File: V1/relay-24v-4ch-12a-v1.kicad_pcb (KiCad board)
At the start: 2 copper layers, 53 x 67.8 mm, 22 parts, among them J1 DG141V-2.54-6P, J2 DB142V-5.08-8P, K1 G5PZ-1A, K2 G5PZ-1A, K3 G5PZ-1A, K4 G5PZ-1A

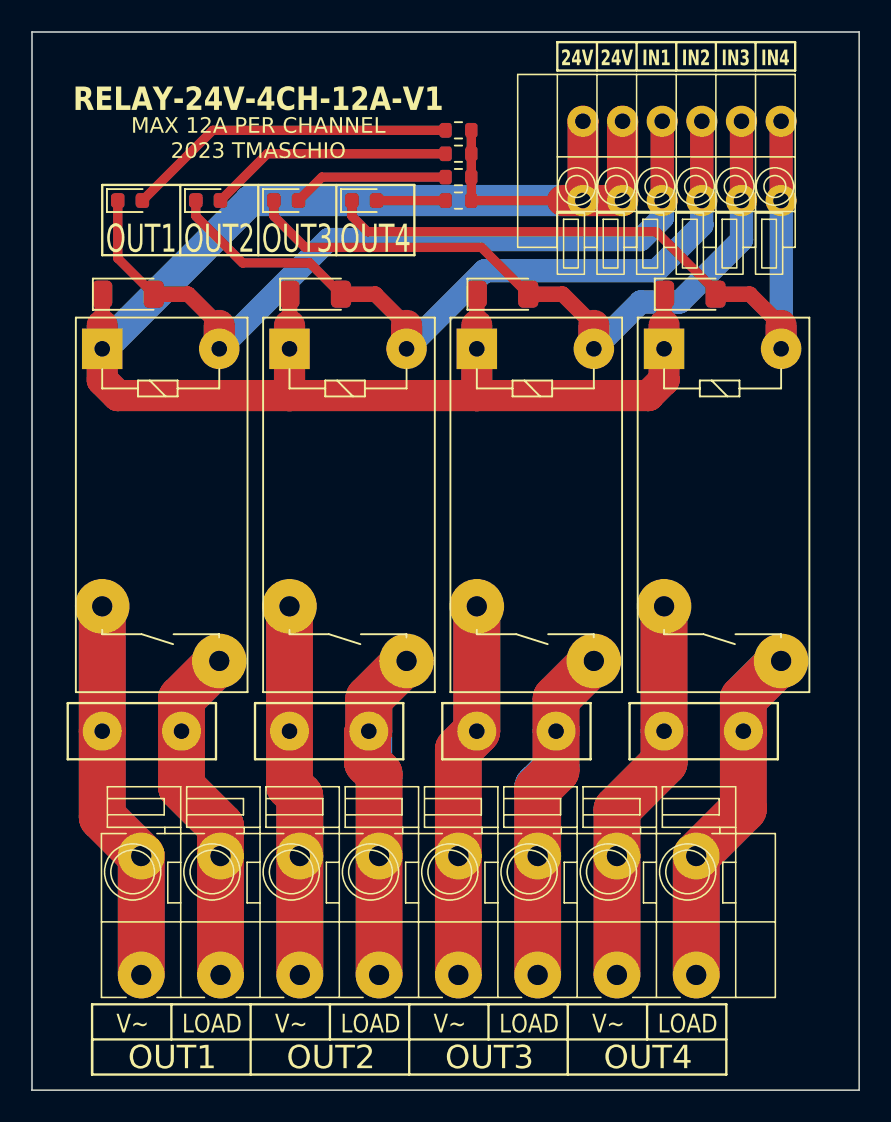
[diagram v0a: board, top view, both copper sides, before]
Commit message: Updated connectors
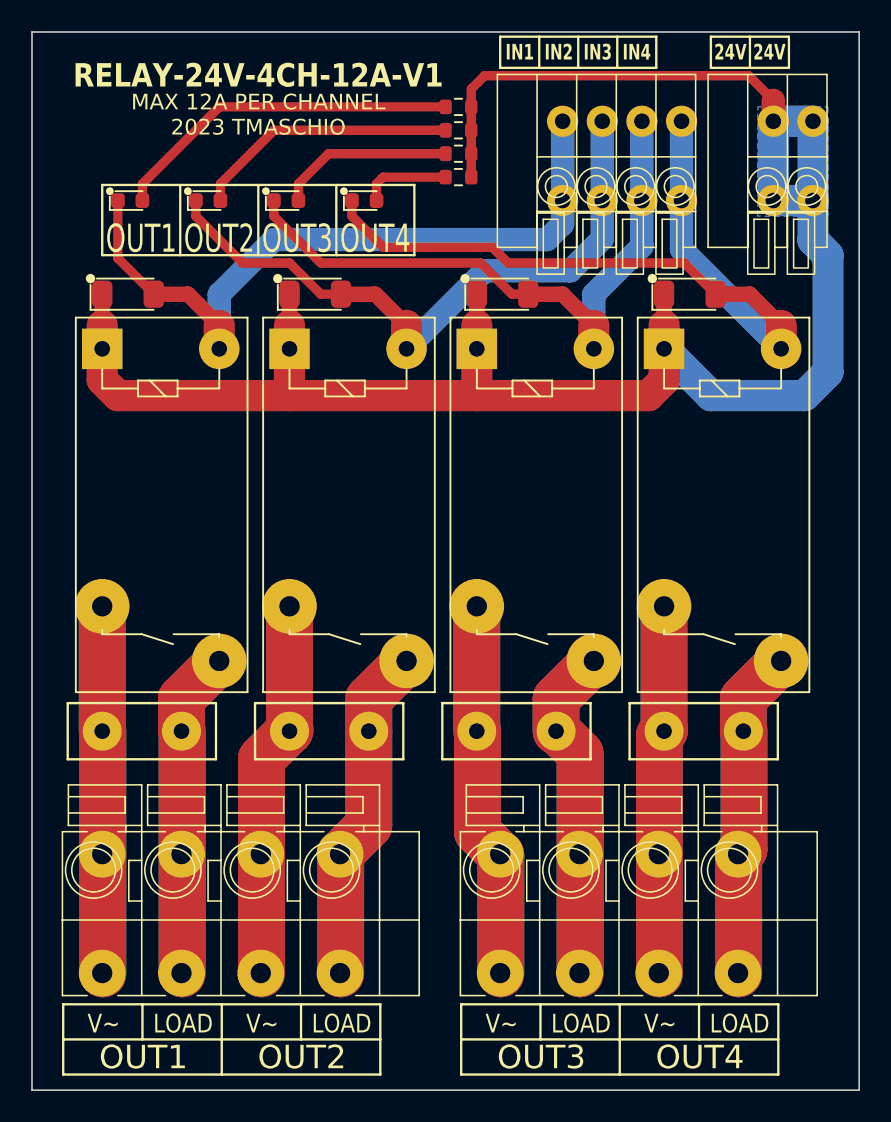
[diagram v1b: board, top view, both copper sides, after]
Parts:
- added J3: DB142V-5.08-4P, Tales:TerminalBlock_Dibo_DB142V-5.08-4P_1x04_P5.08mm_Vertical, F.Cu at (129.5, 122.5)
- added J4: DB142V-5.08-4P, Tales:TerminalBlock_Dibo_DB142V-5.08-4P_1x04_P5.08mm_Vertical, F.Cu at (155.0, 122.5)
- J1: value DG141V-2.54-6P -> DB141V-2.54-2P; footprint Tales:TerminalBlock_Dibo_DB141V-2.54-6P_1x06_P2.54mm_Vertical -> Tales:TerminalBlock_Dibo_DB141V-2.54-2P_1x02_P2.54mm_Vertical
- J2: value DB142V-5.08-8P -> DB141V-2.54-4P; footprint Tales:TerminalBlock_Dibo_DB142V-5.08-8P_1x08_P5.08mm_Vertical -> Tales:TerminalBlock_Dibo_DB141V-2.54-4P_1x04_P2.54mm_Vertical
- R1, R2, R3, R4: value 5k6/100mW -> 6k8/100mW
- moved J2 64.7 mm to (166.6, 67.9), turned to 180 degrees
- moved J1 2.04 mm to (175.0, 67.9)
- moved R1 1.50 mm to (152.3, 67.0)
- moved R2 1.50 mm to (152.3, 68.5)
- moved R3 1.50 mm to (152.3, 70.0)
- moved R4 1.50 mm to (152.3, 71.5)
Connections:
- J1 pad 1: Net-(D7-K) -> +24V
- J1 pad 2: Net-(D5-K) -> +24V
- J2 pad 1: Net-(J2-Pin_1) -> Net-(D7-K)
- J2 pad 2: Net-(J2-Pin_2) -> Net-(D5-K)
- J2 pad 3: Net-(J2-Pin_3) -> Net-(D3-K)
- J2 pad 4: Net-(J2-Pin_4) -> Net-(D1-K)
- K1 pad 2: Net-(J2-Pin_1) -> Net-(J3-Pin_1)
- K1 pad 3: Net-(J2-Pin_2) -> Net-(J3-Pin_2)
- K2 pad 2: Net-(J2-Pin_3) -> Net-(J3-Pin_3)
- K2 pad 3: Net-(J2-Pin_4) -> Net-(J3-Pin_4)
- K3 pad 2: Net-(J2-Pin_5) -> Net-(J4-Pin_1)
- K3 pad 3: Net-(J2-Pin_6) -> Net-(J4-Pin_2)
- K4 pad 2: Net-(J2-Pin_7) -> Net-(J4-Pin_3)
- K4 pad 3: Net-(J2-Pin_8) -> Net-(J4-Pin_4)
- RV1 pad 1: Net-(J2-Pin_1) -> Net-(J3-Pin_1)
- RV1 pad 2: Net-(J2-Pin_2) -> Net-(J3-Pin_2)
- RV2 pad 1: Net-(J2-Pin_3) -> Net-(J3-Pin_3)
- RV2 pad 2: Net-(J2-Pin_4) -> Net-(J3-Pin_4)
- RV3 pad 1: Net-(J2-Pin_5) -> Net-(J4-Pin_1)
- RV3 pad 2: Net-(J2-Pin_6) -> Net-(J4-Pin_2)
- RV4 pad 1: Net-(J2-Pin_7) -> Net-(J4-Pin_3)
- RV4 pad 2: Net-(J2-Pin_8) -> Net-(J4-Pin_4)
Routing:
- net Net-(J2-Pin_7): track 49.7 -> 0.00 mm
- net Net-(J2-Pin_1): track 49.3 -> 0.00 mm
- net Net-(J3-Pin_3): track 0.00 -> 48.8 mm
- net Net-(J4-Pin_1): track 0.00 -> 48.5 mm
- net Net-(J2-Pin_5): track 48.2 -> 0.00 mm
- net Net-(J2-Pin_3): track 47.8 -> 0.00 mm
- net Net-(J4-Pin_3): track 0.00 -> 47.5 mm
- net Net-(J3-Pin_1): track 0.00 -> 47.2 mm
- net Net-(J2-Pin_8): track 44.7 -> 0.00 mm
- net Net-(J2-Pin_2): track 44.3 -> 0.00 mm
- net Net-(J3-Pin_4): track 0.00 -> 43.5 mm
- net Net-(J4-Pin_2): track 0.00 -> 43.5 mm
- net Net-(J2-Pin_6): track 43.2 -> 0.00 mm
- net Net-(J2-Pin_4): track 42.9 -> 0.00 mm
- net Net-(J4-Pin_4): track 0.00 -> 42.5 mm
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- added copper zone on B.Cu, net +24V

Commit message: Revision before manufacturing
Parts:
- D1, D3, D5, D7: value GREEN -> WHITE
- R1, R2, R3, R4: value 6k8/100mW -> 10k/100mW
- moved K1 10.7 mm to (133.2, 92.5)
- moved K2 10.7 mm to (145.2, 92.5)
- moved K3 10.7 mm to (157.2, 92.5)
- moved K4 10.7 mm to (169.2, 92.5)
- moved J3 8.61 mm to (137.2, 118.8)
- moved J4 8.61 mm to (162.8, 118.8)
- moved J2 4.65 mm to (162.8, 70.5)
- moved J1 2.88 mm to (173.8, 70.5)
- moved RV1 2.75 mm to (132.2, 107.0)
- moved RV2 2.75 mm to (144.2, 107.0)
- moved RV3 2.75 mm to (156.2, 107.0)
- moved RV4 2.75 mm to (168.2, 107.0)
- moved D2 0.15 mm to (131.0, 79.0)
- moved D4 0.15 mm to (143.0, 79.0)
- moved D6 0.15 mm to (155.0, 79.0)
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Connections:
- net Net-(D1-A) renamed /LED1
- net Net-(D1-K) renamed /IN1
- net Net-(D3-A) renamed /LED2
- net Net-(D3-K) renamed /IN2
- net Net-(D5-A) renamed /LED3
- net Net-(D5-K) renamed /IN3
- net Net-(D7-A) renamed /LED4
- net Net-(D7-K) renamed /IN4
- net Net-(J3-Pin_1) renamed /OUT1PW
- net Net-(J3-Pin_2) renamed /OUT1LD
- net Net-(J3-Pin_3) renamed /OUT2PW
- net Net-(J3-Pin_4) renamed /OUT2LD
- net Net-(J4-Pin_1) renamed /OUT3PW
- net Net-(J4-Pin_2) renamed /OUT3LD
- net Net-(J4-Pin_3) renamed /OUT4PW
- net Net-(J4-Pin_4) renamed /OUT4LD
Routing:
- net +24V: track 127.2 -> 115.2 mm
- net /IN2: track 41.9 -> 43.7 mm
- net /IN1: track 47.4 -> 46.8 mm
- net /LED3: track 11.3 -> 10.7 mm
- net /LED4: track 5.68 -> 5.08 mm
- net /LED2: track 16.9 -> 16.3 mm
- net /LED1: track 22.5 -> 21.9 mm
- added copper zone on F.Cu, net +24V
- removed copper zone on B.Cu, net +24V
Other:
- rule pad_to_mask_clearance: 0 -> 0.1

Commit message: Review before fabrication
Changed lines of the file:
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@@
 			(unlocked yes)
 			(layer "F.SilkS")
-			(hide yes)
 			(effects
 				(font
@@
 			)
 		)
-		(property "JLCPCB BOM" "0"
+		(property "JLCPCB BOM" "1"
 			(at 83 248 0)
 			(layer "F.Fab")
@@
 			)
 		)
-		(property "Mfr PN" "G5PZ-1A"
+		(property "Mfr PN" "G5PZ-1A-E DC24V"
 			(at 83 248 0)
 			(layer "F.Fab")
@@
 			)
 		)
-		(property "Vendor" "Mouser"
+		(property "Vendor" "JLCPCB"
 			(at 83 248 0)
 			(layer "F.Fab")
@@
 			)
 		)
-		(property "Vendor PN" "653-G5PZ-1ADC24"
+		(property "Vendor PN" "C6719448"
 			(at 83 248 0)
 			(layer "F.Fab")
@@
 			)
 		)
+		(property "LCSC Part #" "C6719448"
+			(at 0 0 270)
+			(unlocked yes)
+			(layer "F.Fab")
+			(hide yes)
+			(effects
+				(font
+					(size 1 1)
+					(thickness 0.15)
+				)
+			)
+		)
 		(property ki_fp_filters "Relay*SPST*Omron*G5PZ*")
 		(sheetname "/")
@@
 			(at 6 -1.25 0)
 			(layer "F.SilkS")
-			(hide yes)
 			(effects
 				(font
@@
 			)
 		)
+		(property "LCSC Part #" "C2898744"
+			(at 0 0 180)
+			(unlocked yes)
+			(layer "F.Fab")
+			(hide yes)
+			(effects
+				(font
+					(size 1 1)
+					(thickness 0.15)
+				)
+			)
+		)
+		(property "Mfr" "DORABO"
+			(at 0 0 180)
+			(unlocked yes)
+			(layer "F.Fab")
+			(hide yes)
+			(effects
+				(font
+					(size 1 1)
+					(thickness 0.15)
+				)
+			)
+		)
+		(property "Mfr PN" "DB141V-2.54-2P-GN"
+			(at 0 0 180)
+			(unlocked yes)
+			(layer "F.Fab")
+			(hide yes)
+			(effects
+				(font
+					(size 1 1)
+					(thickness 0.15)
+				)
+			)
+		)
+		(property "Vendor PN" "C2898744"
+			(at 0 0 180)
+			(unlocked yes)
+			(layer "F.Fab")
+			(hide yes)
+			(effects
+				(font
+					(size 1 1)
+					(thickness 0.15)
+				)
+			)
+		)
 		(property ki_fp_filters "Connector*:*_1x??_*")
 		(sheetname "/")
@@
 			)
 		)
-		(property "JLCPCB BOM" "0"
+		(property "JLCPCB BOM" "1"
 			(at 71 236 0)
 			(layer "F.Fab")
@@
 			)
 		)
-		(property "Mfr PN" "G5PZ-1A"
+		(property "Mfr PN" "G5PZ-1A-E DC24V"
 			(at 71 236 0)
 			(layer "F.Fab")
@@
 			)
 		)
-		(property "Vendor" "Mouser"
+		(property "Vendor" "JLCPCB"
 			(at 71 236 0)
 			(layer "F.Fab")
@@
 			)
 		)
-		(property "Vendor PN" "653-G5PZ-1ADC24"
+		(property "Vendor PN" "C6719448"
 			(at 71 236 0)
 			(layer "F.Fab")
@@
 			)
 		)
+		(property "LCSC Part #" "C6719448"
+			(at 0 0 270)
+			(unlocked yes)
+			(layer "F.Fab")
+			(hide yes)
+			(effects
+				(font
+					(size 1 1)
+					(thickness 0.15)
+				)
+			)
+		)
 		(property ki_fp_filters "Relay*SPST*Omron*G5PZ*")
 		(sheetname "/")
@@
 			(at 6 -1.25 0)
 			(layer "F.SilkS")
-			(hide yes)
 			(effects
 				(font
@@
 			(at 6 -1.25 0)
 			(layer "F.SilkS")
-			(hide yes)
 			(effects
 				(font
@@
 			(unlocked yes)
 			(layer "F.SilkS")
-			(hide yes)
 			(effects
 				(font
@@
 			)
 		)
+		(property "LCSC Part #" "C2898746"
+			(at 0 0 180)
+			(unlocked yes)
+			(layer "F.Fab")
+			(hide yes)
+			(effects
+				(font
+					(size 1 1)
+					(thickness 0.15)
+				)
+			)
+		)
+		(property "Mfr" "DORABO"
+			(at 0 0 180)
+			(unlocked yes)
+			(layer "F.Fab")
+			(hide yes)
+			(effects
+				(font
+					(size 1 1)
+					(thickness 0.15)
+				)
+			)
+		)
+		(property "Mfr PN" "DB141V-2.54-4P-GN"
+			(at 0 0 180)
+			(unlocked yes)
+			(layer "F.Fab")
+			(hide yes)
+			(effects
+				(font
+					(size 1 1)
+					(thickness 0.15)
+				)
+			)
+		)
+		(property "Vendor PN" "C2898746"
+			(at 0 0 180)
+			(unlocked yes)
+			(layer "F.Fab")
+			(hide yes)
+			(effects
+				(font
+					(size 1 1)
+					(thickness 0.15)
+				)
+			)
+		)
 		(property ki_fp_filters "Connector*:*_1x??_*")
 		(sheetname "/")
@@
 			)
 		)
-		(property "JLCPCB BOM" "0"
+		(property "JLCPCB BOM" "1"
 			(at 59 224 0)
 			(layer "F.Fab")
@@
 			)
 		)
-		(property "Mfr PN" "G5PZ-1A"
+		(property "Mfr PN" "G5PZ-1A-E DC24V"
 			(at 59 224 0)
 			(layer "F.Fab")
@@
 			)
 		)
-		(property "Vendor" "Mouser"
+		(property "Vendor" "JLCPCB"
 			(at 59 224 0)
 			(layer "F.Fab")
@@
 			)
 		)
-		(property "Vendor PN" "653-G5PZ-1ADC24"
+		(property "Vendor PN" "C6719448"
 			(at 59 224 0)
 			(layer "F.Fab")
@@
 			)
 		)
+		(property "LCSC Part #" "C6719448"
+			(at 0 0 270)
+			(unlocked yes)
+			(layer "F.Fab")
+			(hide yes)
+			(effects
+				(font
+					(size 1 1)
+					(thickness 0.15)
+				)
+			)
+		)
 		(property ki_fp_filters "Relay*SPST*Omron*G5PZ*")
 		(sheetname "/")
@@
 			)
 		)
-		(property "JLCPCB BOM" "0"
+		(property "JLCPCB BOM" "1"
 			(at 47 212 0)
 			(layer "F.Fab")
@@
 			)
 		)
-		(property "Mfr PN" "G5PZ-1A"
+		(property "Mfr PN" "G5PZ-1A-E DC24V"
 			(at 47 212 0)
 			(layer "F.Fab")
@@
 			)
 		)
-		(property "Vendor" "Mouser"
+		(property "Vendor" "JLCPCB"
 			(at 47 212 0)
 			(layer "F.Fab")
@@
 			)
 		)
-		(property "Vendor PN" "653-G5PZ-1ADC24"
+		(property "Vendor PN" "C6719448"
 			(at 47 212 0)
 			(layer "F.Fab")
@@
 			)
 		)
+		(property "LCSC Part #" "C6719448"
+			(at 0 0 270)
+			(unlocked yes)
+			(layer "F.Fab")
+			(hide yes)
+			(effects
+				(font
+					(size 1 1)
+					(thickness 0.15)
+				)
+			)
+		)
 		(property ki_fp_filters "Relay*SPST*Omron*G5PZ*")
 		(sheetname "/")
@@
 			(at 6 -1.25 0)
 			(layer "F.SilkS")
-			(hide yes)
 			(effects
 				(font
@@
 		(effects
 			(font
-				(size 1.5 1.5)
+				(size 1.4 1.3)
 				(thickness 0.2)
 			)
@@
 		(effects
 			(font
-				(size 1.5 1.5)
+				(size 1.4 1.3)
 				(thickness 0.2)
 			)
@@
 		(effects
 			(font
-				(size 1.5 1.5)
+				(size 1.4 1.3)
 				(thickness 0.2)
 			)
@@
 		(effects
 			(font
-				(size 1.5 1.5)
+				(size 1.4 1.3)
 				(thickness 0.2)
 			)

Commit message: Revising before manufacturing.
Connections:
- net /OUT1PW renamed /OUT1LN
- net /OUT2PW renamed /OUT2LN
- net /OUT3PW renamed /OUT3LN
- net /OUT4PW renamed /OUT4LN
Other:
- board text added: "LINE"
- board text removed: "V~"
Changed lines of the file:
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@@
 	(net 8 "/LED4")
 	(net 9 "/IN4")
-	(net 10 "/OUT1PW")
+	(net 10 "/OUT2LN")
 	(net 11 "/OUT2LD")
 	(net 12 "/OUT1LD")
-	(net 13 "/OUT2PW")
+	(net 13 "/OUT1LN")
 	(net 14 "/OUT3LD")
-	(net 15 "/OUT3PW")
+	(net 15 "/OUT3LN")
 	(net 16 "/OUT4LD")
-	(net 17 "/OUT4PW")
+	(net 17 "/OUT4LN")
 	(footprint "Tales:TerminalBlock_Dibo_DB142V-5.08-4P_1x04_P5.08mm_Vertical"
 		(layer "F.Cu")
@@
 			(layers "*.Cu" "*.Mask")
 			(remove_unused_layers no)
-			(net 15 "/OUT3PW")
+			(net 15 "/OUT3LN")
 			(pinfunction "Pin_1")
 			(pintype "passive")
@@
 			(layers "*.Cu" "*.Mask")
 			(remove_unused_layers no)
-			(net 15 "/OUT3PW")
+			(net 15 "/OUT3LN")
 			(pinfunction "Pin_1")
 			(pintype "passive")
@@
 			(layers "*.Cu" "*.Mask")
 			(remove_unused_layers no)
-			(net 17 "/OUT4PW")
+			(net 17 "/OUT4LN")
 			(pinfunction "Pin_3")
 			(pintype "passive")
@@
 			(layers "*.Cu" "*.Mask")
 			(remove_unused_layers no)
-			(net 17 "/OUT4PW")
+			(net 17 "/OUT4LN")
 			(pinfunction "Pin_3")
 			(pintype "passive")
@@
 			(layers "*.Cu" "*.Mask")
 			(remove_unused_layers no)
-			(net 17 "/OUT4PW")
+			(net 17 "/OUT4LN")
 			(pintype "passive")
 		)
@@
 			(layers "*.Cu" "*.Mask")
 			(remove_unused_layers no)
-			(net 10 "/OUT1PW")
+			(net 13 "/OUT1LN")
 			(pintype "passive")
 		)
@@
 			(layers "*.Cu" "*.Mask")
 			(remove_unused_layers no)
-			(net 15 "/OUT3PW")
+			(net 15 "/OUT3LN")
 			(pintype "passive")
 		)
@@
 			(layers "*.Cu" "*.Mask")
 			(remove_unused_layers no)
-			(net 17 "/OUT4PW")
+			(net 17 "/OUT4LN")
 			(pintype "passive")
 		)
@@
 			(layers "*.Cu" "*.Mask")
 			(remove_unused_layers no)
-			(net 13 "/OUT2PW")
+			(net 10 "/OUT2LN")
 			(pintype "passive")
 		)
@@
 			(layers "*.Cu" "*.Mask")
 			(remove_unused_layers no)
-			(net 10 "/OUT1PW")
+			(net 13 "/OUT1LN")
 			(pinfunction "Pin_1")
 			(pintype "passive")
@@
 			(layers "*.Cu" "*.Mask")
 			(remove_unused_layers no)
-			(net 10 "/OUT1PW")
+			(net 13 "/OUT1LN")
 			(pinfunction "Pin_1")
 			(pintype "passive")
@@
 			(layers "*.Cu" "*.Mask")
 			(remove_unused_layers no)
-			(net 13 "/OUT2PW")
+			(net 10 "/OUT2LN")
 			(pinfunction "Pin_3")
 			(pintype "passive")
@@
 			(layers "*.Cu" "*.Mask")
 			(remove_unused_layers no)
-			(net 13 "/OUT2PW")
+			(net 10 "/OUT2LN")
 			(pinfunction "Pin_3")
 			(pintype "passive")
@@
 			(layers "*.Cu" "*.Mask")
 			(remove_unused_layers no)
-			(net 13 "/OUT2PW")
+			(net 10 "/OUT2LN")
 			(pintype "passive")
 		)
@@
 			(layers "*.Cu" "*.Mask")
 			(remove_unused_layers no)
-			(net 10 "/OUT1PW")
+			(net 13 "/OUT1LN")
 			(pintype "passive")
 		)
@@
 			(layers "*.Cu" "*.Mask")
 			(remove_unused_layers no)
-			(net 15 "/OUT3PW")
+			(net 15 "/OUT3LN")
 			(pintype "passive")
 		)
@@
 		)
 	)
-	(gr_text "V~"
+	(gr_text "LINE"
 		(at 155.1 125.75 0)
 		(layer "F.SilkS")
@@
 		)
 	)
-	(gr_text "V~"
+	(gr_text "LINE"
 		(at 129.6 125.75 0)
 		(layer "F.SilkS")
@@
 		)
 	)
-	(gr_text "V~"
+	(gr_text "LINE"
 		(at 165.26 125.75 0)
 		(layer "F.SilkS")
@@
 		)
 	)
-	(gr_text "V~"
+	(gr_text "LINE"
 		(at 139.76 125.75 0)
 		(layer "F.SilkS")
@@
 	)
 	(segment
-		(start 129.63 114.94)
-		(end 129.63 107.08)
+		(start 139.79 122.56)
+		(end 139.79 114.94)
 		(width 3)
 		(layer "F.Cu")
@@
 	)
 	(segment
-		(start 129.71 107)
-		(end 129.71 99.21)
+		(start 139.79 114.94)
+		(end 139.79 108.92)
 		(width 3)
 		(layer "F.Cu")
@@
 	)
 	(segment
-		(start 129.63 122.56)
-		(end 129.63 114.94)
+		(start 139.79 108.92)
+		(end 141.71 107)
 		(width 3)
 		(layer "F.Cu")
@@
 	)
 	(segment
-		(start 129.63 107.08)
-		(end 129.71 107)
+		(start 141.71 107)
+		(end 141.71 99.21)
 		(width 3)
 		(layer "F.Cu")
@@
 	)
 	(segment
-		(start 129.71 99.21)
-		(end 129.5 99)
+		(start 141.71 99.21)
+		(end 141.5 99)
 		(width 3)
 		(layer "F.Cu")
@@
 	)
 	(segment
-		(start 129.71 107)
-		(end 129.71 99.21)
+		(start 141.71 107)
+		(end 141.71 99.21)
 		(width 3)
 		(layer "B.Cu")
@@
 	)
 	(segment
-		(start 129.63 122.56)
-		(end 129.63 114.94)
+		(start 139.79 108.92)
+		(end 141.71 107)
 		(width 3)
 		(layer "B.Cu")
@@
 	)
 	(segment
-		(start 129.63 107.08)
-		(end 129.71 107)
+		(start 141.71 99.21)
+		(end 141.5 99)
 		(width 3)
 		(layer "B.Cu")
@@
 	)
 	(segment
-		(start 129.71 99.21)
-		(end 129.5 99)
+		(start 139.79 122.56)
+		(end 139.79 114.94)
 		(width 3)
 		(layer "B.Cu")
@@
 	)
 	(segment
-		(start 129.63 114.94)
-		(end 129.63 107.08)
+		(start 139.79 114.94)
+		(end 139.79 108.92)
 		(width 3)
 		(layer "B.Cu")
@@
 	)
 	(segment
-		(start 139.79 122.56)
-		(end 139.79 114.94)
+		(start 129.63 114.94)
+		(end 129.63 107.08)
 		(width 3)
 		(layer "F.Cu")
@@
 	)
 	(segment
-		(start 139.79 114.94)
-		(end 139.79 108.92)
+		(start 129.71 107)
+		(end 129.71 99.21)
 		(width 3)
 		(layer "F.Cu")
@@
 	)
 	(segment
-		(start 139.79 108.92)
-		(end 141.71 107)
+		(start 129.63 122.56)
+		(end 129.63 114.94)
 		(width 3)
 		(layer "F.Cu")
@@
 	)
 	(segment
-		(start 141.71 107)
-		(end 141.71 99.21)
+		(start 129.63 107.08)
+		(end 129.71 107)
 		(width 3)
 		(layer "F.Cu")
@@
 	)
 	(segment
-		(start 141.71 99.21)
-		(end 141.5 99)
+		(start 129.71 99.21)
+		(end 129.5 99)
 		(width 3)
 		(layer "F.Cu")
@@
 	)
 	(segment
-		(start 141.71 107)
-		(end 141.71 99.21)
+		(start 129.71 107)
+		(end 129.71 99.21)
 		(width 3)
 		(layer "B.Cu")
@@
 	)
 	(segment
-		(start 139.79 108.92)
-		(end 141.71 107)
+		(start 129.63 122.56)
+		(end 129.63 114.94)
 		(width 3)
 		(layer "B.Cu")
@@
 	)
 	(segment
-		(start 141.71 99.21)
-		(end 141.5 99)
+		(start 129.63 107.08)
+		(end 129.71 107)
 		(width 3)
 		(layer "B.Cu")
@@
 	)
 	(segment
-		(start 139.79 122.56)
-		(end 139.79 114.94)
+		(start 129.71 99.21)
+		(end 129.5 99)
 		(width 3)
 		(layer "B.Cu")
@@
 	)
 	(segment
-		(start 139.79 114.94)
-		(end 139.79 108.92)
+		(start 129.63 114.94)
+		(end 129.63 107.08)
 		(width 3)
 		(layer "B.Cu")
